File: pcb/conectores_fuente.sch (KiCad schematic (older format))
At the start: 31 parts, among them J1 UJ2-MIBH-G-SMT-TR, J2 Conn_01x03, J3 Conn_02x05_Odd_Even, J4 Conn_01x03, J5 Conn_01x03, J6 Conn_02x03_Odd_Even, Q1 MMSS8050-H-TP, Q2 MMSS8050-H-TP, Q3 AO3401A, U1 LD1117S33TR_SOT223

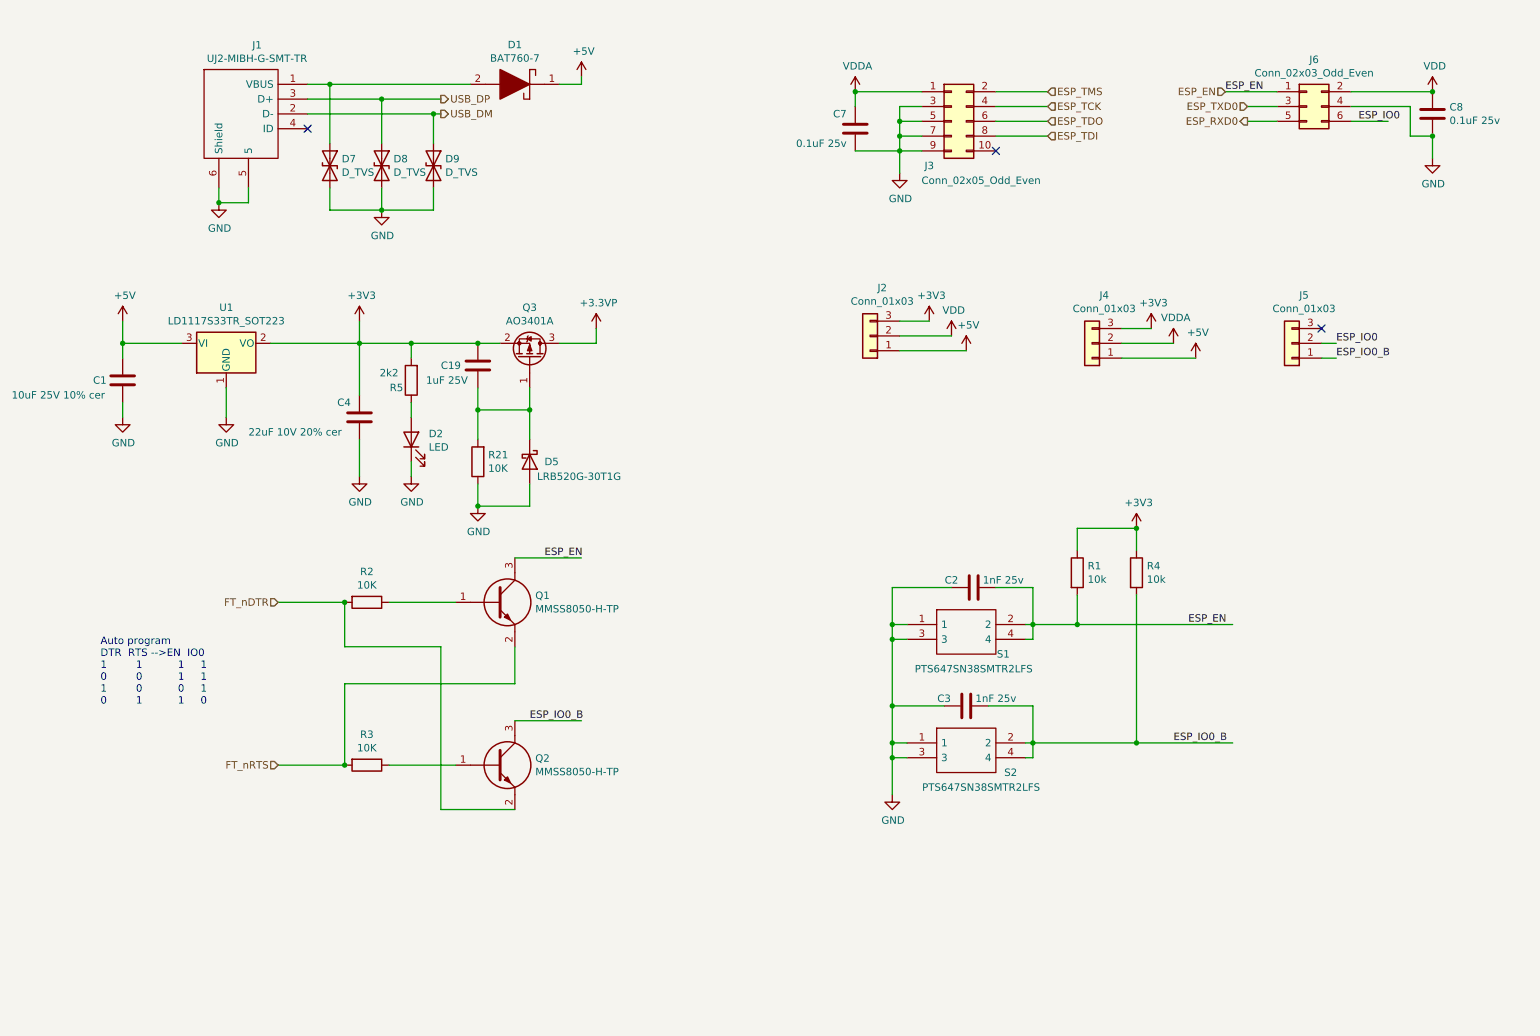
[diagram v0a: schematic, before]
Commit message: se agregan notas aclaratorias a los esquemáticos
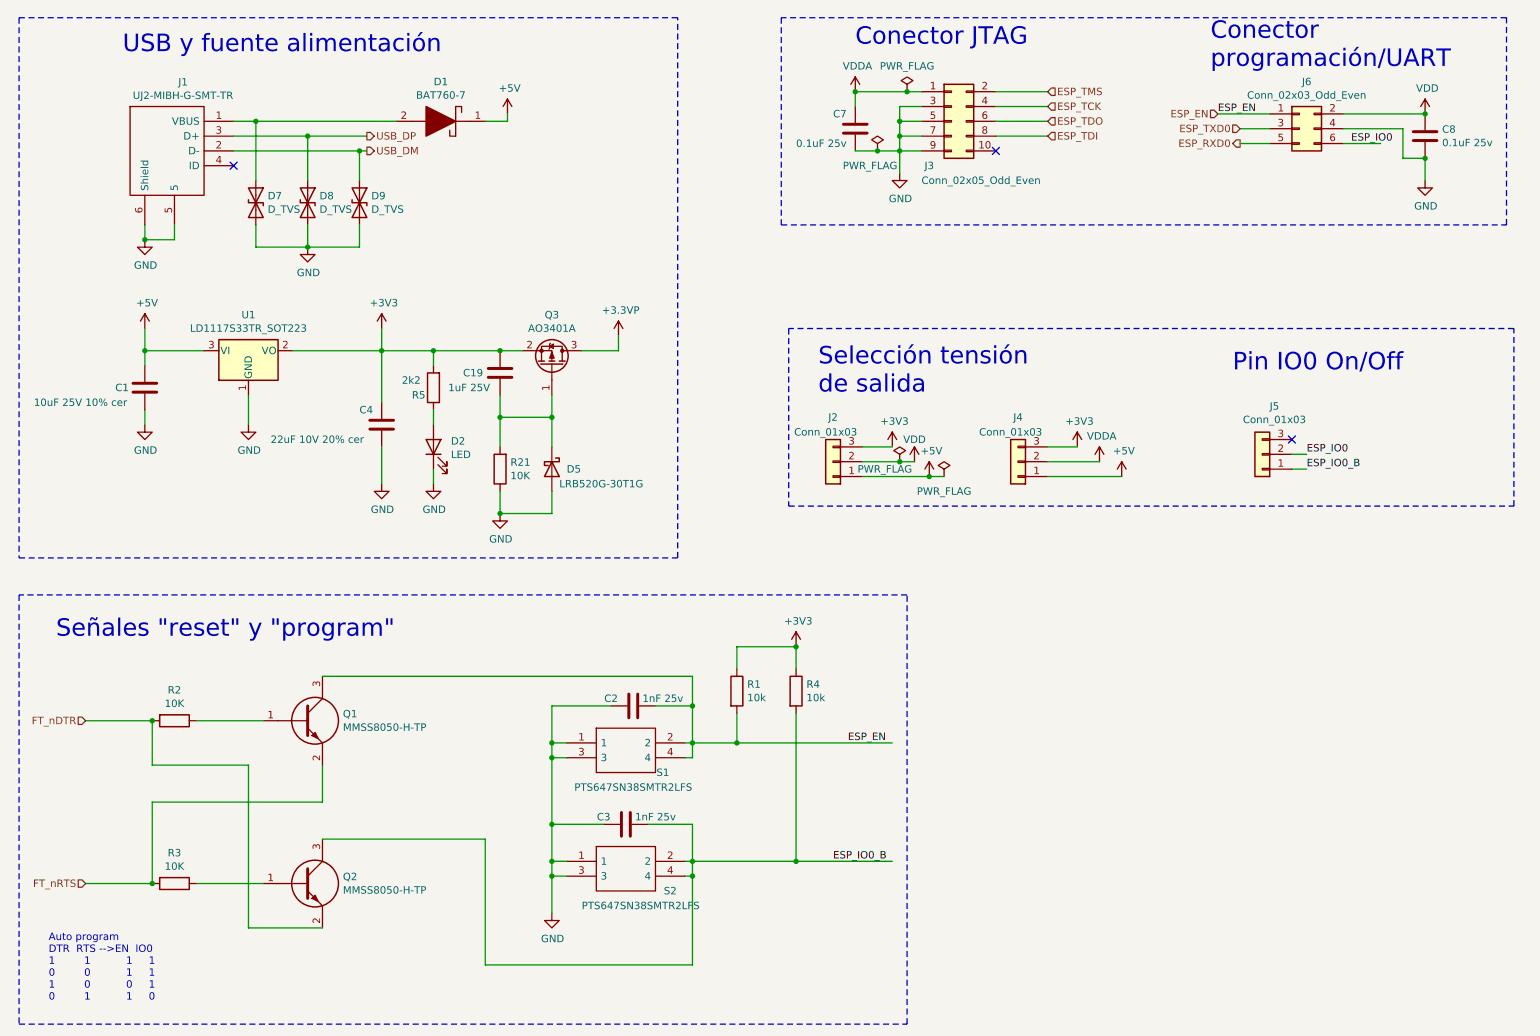
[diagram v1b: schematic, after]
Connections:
- wire segments 120 -> 128
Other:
- note added: "Conector JTAG"
- note added: "Conector \nprogramación/UART"
- note added: "Pin IO0 On/Off"
- note added: "Selección tensión \nde salida"
- note added: "Señales "reset" y "program""
- note added: "USB y fuente alimentación"
- moved on the sheet: C1, C19, C2, C3, C4, C8, D1, D2, D5, D7, D8, D9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

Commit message: avances en el pcb y correcciones al esquematico
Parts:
- J6: footprint Connector_PinHeader_1.27mm:PinHeader_2x05_P1.27mm_Vertical_SMD -> Connector_PinHeader_1.27mm:PinHeader_2x03_P1.27mm_Vertical_SMD
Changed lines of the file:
@@
 F 0 "J6" H 9450 1867 50  0000 C CNN
 F 1 "Conn_02x03_Odd_Even" H 9450 1776 50  0000 C CNN
-F 2 "Connector_PinHeader_1.27mm:PinHeader_2x05_P1.27mm_Vertical_SMD" H 9400 1550 50  0001 C CNN
+F 2 "Connector_PinHeader_1.27mm:PinHeader_2x03_P1.27mm_Vertical_SMD" H 9400 1550 50  0001 C CNN
 F 3 "~" H 9400 1550 50  0001 C CNN
 	1    9400 1550

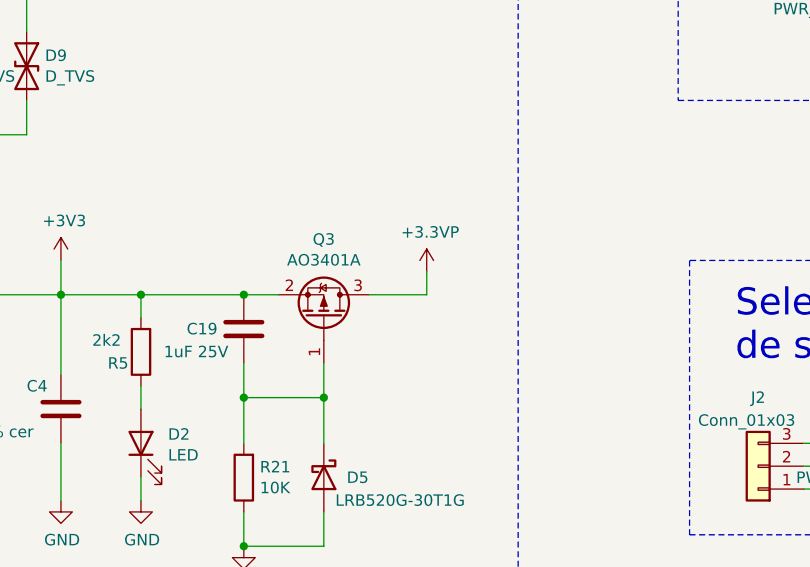
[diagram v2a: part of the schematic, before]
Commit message: Primer versión ruteo terminada
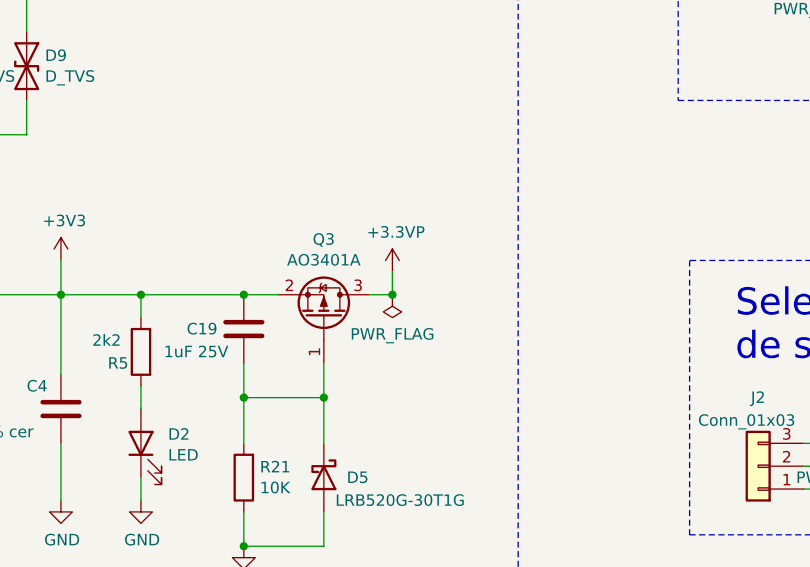
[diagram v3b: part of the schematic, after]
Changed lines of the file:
@@
 	4000 3050 3550 3050
 Connection ~ 4000 3050
-Wire Wire Line
-	4550 3050 4800 3050
-Wire Wire Line
-	4800 3050 4800 2950
-$Comp
-L power:+3.3VP #PWR?
-U 1 1 61231E82
-P 4800 2950
-AR Path="/60E64650/61231E82" Ref="#PWR?"  Part="1"
-AR Path="/61231E82" Ref="#PWR?"  Part="1"
-AR Path="/6120E92C/61231E82" Ref="#PWR0124"  Part="1"
-F 0 "#PWR0124" H 4950 2900 50  0001 C CNN
-F 1 "+3.3VP" H 4815 3123 50  0000 C CNN
-F 2 "" H 4800 2950 50  0001 C CNN
-F 3 "" H 4800 2950 50  0001 C CNN
-	1    4800 2950
-	1    0    0    -1
-$EndComp
 $Comp
 L power:+3V3 #PWR?
@@
 Wire Wire Line
 	6750 1300 6850 1300
+$Comp
+L power:+3.3VP #PWR0124
+U 1 1 6132E8AD
+P 4650 2950
+F 0 "#PWR0124" H 4800 2900 50  0001 C CNN
+F 1 "+3.3VP" H 4665 3123 50  0000 C CNN
+F 2 "" H 4650 2950 50  0001 C CNN
+F 3 "" H 4650 2950 50  0001 C CNN
+	1    4650 2950
+	1    0    0    -1
+$EndComp
+Wire Wire Line
+	4550 3050 4650 3050
+Wire Wire Line
+	4650 3050 4650 2950
+$Comp
+L power:PWR_FLAG #FLG0101
+U 1 1 61333E06
+P 4650 3050
+F 0 "#FLG0101" H 4650 3125 50  0001 C CNN
+F 1 "PWR_FLAG" H 4650 3223 50  0000 C CNN
+F 2 "" H 4650 3050 50  0001 C CNN
+F 3 "~" H 4650 3050 50  0001 C CNN
+	1    4650 3050
+	-1   0    0    1
+$EndComp
+Connection ~ 4650 3050
 $EndSCHEMATC
